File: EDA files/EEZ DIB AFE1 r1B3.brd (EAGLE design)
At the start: 141.5 x 68.5 mm, 198 parts, among them IC1 OPA4202IPWR, IC10 N.C., IC11 N.C., IC12 N.C., IC13 ADS131E04IPAGR, IC14 TPS71725DCKR, IC15 TPS72325DBVR, IC2 DG212BDY-T1-E3, IC3 ULN2803ADWR, IC4 OPA4202IPWR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

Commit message: small PCB layout changes
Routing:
- net GND: track 88.3 -> 86.8 mm, vias 66 -> 67
- net IN3P: track 39.7 -> 39.5 mm, vias 3 -> 2
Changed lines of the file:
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@@
 <layer number="13" name="Route13" color="4" fill="5" visible="no" active="no"/>
 <layer number="14" name="Route14" color="1" fill="6" visible="no" active="no"/>
-<layer number="15" name="Power" color="6" fill="1" visible="no" active="yes"/>
-<layer number="16" name="Bottom" color="1" fill="1" visible="no" active="yes"/>
+<layer number="15" name="Power" color="6" fill="1" visible="yes" active="yes"/>
+<layer number="16" name="Bottom" color="1" fill="1" visible="yes" active="yes"/>
 <layer number="17" name="Pads" color="14" fill="1" visible="yes" active="yes"/>
 <layer number="18" name="Vias" color="6" fill="1" visible="yes" active="yes"/>
@@
 <layer number="37" name="tTest" color="7" fill="1" visible="no" active="yes"/>
 <layer number="38" name="bTest" color="7" fill="1" visible="no" active="yes"/>
-<layer number="39" name="tKeepout" color="15" fill="1" visible="yes" active="yes"/>
+<layer number="39" name="tKeepout" color="15" fill="1" visible="no" active="yes"/>
 <layer number="40" name="bKeepout" color="5" fill="1" visible="no" active="yes"/>
 <layer number="41" name="tRestrict" color="4" fill="10" visible="no" active="yes"/>
@@
 <via x="55.4228" y="43.2181" extent="1-16" drill="0.4" shape="square"/>
 <via x="54.3941" y="41.6306" extent="1-16" drill="0.4" shape="square"/>
-<wire x1="102.2096" y1="40.9804" x2="105.0061" y2="40.9804" width="0.2032" layer="1"/>
 <wire x1="105.0061" y1="40.9804" x2="105.1941" y2="40.7924" width="0.2032" layer="1"/>
 <wire x1="124.5226" y1="21.5646" x2="124.5226" y2="20.7273" width="0.2032" layer="1"/>
@@
 <via x="89.9033" y="13.2715" extent="1-16" drill="0.4" shape="square"/>
 <contactref element="IC13" pad="41"/>
+<via x="103.1875" y="41.8592" extent="1-16" drill="0.4" shape="octagon"/>
+<wire x1="102.2096" y1="40.9804" x2="102.3087" y2="40.9804" width="0.254" layer="1"/>
+<wire x1="102.3087" y1="40.9804" x2="103.1875" y2="41.8592" width="0.254" layer="1"/>
 <wire x1="105.1814" y1="6.7818" x2="105.2004" y2="6.7867" width="0" layer="19" extent="1-1"/>
 <wire x1="104.3504" y1="5.1117" x2="104.3686" y2="5.1308" width="0" layer="19" extent="1-1"/>
@@
 <wire x1="77.4954" y1="27.4828" x2="77.4954" y2="29.6418" width="0.8128" layer="16"/>
 <wire x1="77.4954" y1="29.6418" x2="79.756" y2="31.9024" width="0.8128" layer="16"/>
-<wire x1="103.1875" y1="31.9024" x2="103.1875" y2="42.6593" width="0.8128" layer="15"/>
-<wire x1="103.1875" y1="42.6593" x2="101.3714" y2="44.4754" width="0.8128" layer="15"/>
+<wire x1="103.1875" y1="31.9024" x2="103.1875" y2="38.7477" width="0.8128" layer="15"/>
 <wire x1="98.552" y1="48.2346" x2="93.7641" y2="48.2346" width="0.508" layer="16"/>
 <wire x1="93.7641" y1="48.2346" x2="93.6371" y2="48.1076" width="0.508" layer="16"/>
 <wire x1="101.3714" y1="44.4754" x2="101.3714" y2="45.4152" width="0.508" layer="16"/>
 <wire x1="101.3714" y1="45.4152" x2="98.552" y2="48.2346" width="0.508" layer="16"/>
+<wire x1="101.3714" y1="44.4754" x2="101.3714" y2="40.5638" width="0.8128" layer="15"/>
+<wire x1="101.3714" y1="40.5638" x2="103.1875" y2="38.7477" width="0.8128" layer="15"/>
 </signal>
 <signal name="+3V3_ISO">
@@
 <wire x1="89.8271" y1="47.9171" x2="91.0971" y2="46.6471" width="0.2032" layer="1"/>
 <wire x1="91.0971" y1="46.609" x2="91.0971" y2="46.6471" width="0.2032" layer="1"/>
-<wire x1="90.4748" y1="44.3611" x2="90.9701" y2="44.8564" width="0.2032" layer="1"/>
-<wire x1="90.9701" y1="44.8564" x2="91.0971" y2="45.4787" width="0.2032" layer="1"/>
-<wire x1="86.7029" y1="40.8305" x2="88.2396" y2="42.3672" width="0.2032" layer="1"/>
-<wire x1="90.4748" y1="44.3611" x2="88.9381" y2="44.3611" width="0.2032" layer="1"/>
-<wire x1="88.9381" y1="44.3611" x2="88.2396" y2="43.6626" width="0.2032" layer="1"/>
-<wire x1="88.2396" y1="42.3672" x2="88.2396" y2="43.6626" width="0.2032" layer="1"/>
-<via x="90.932" y="44.5897" extent="1-16" drill="0.4" shape="octagon"/>
-<wire x1="90.9701" y1="44.8564" x2="90.9701" y2="44.6278" width="0.2032" layer="1"/>
-<wire x1="90.9701" y1="44.6278" x2="90.932" y2="44.5897" width="0.2032" layer="1"/>
+<wire x1="86.7029" y1="40.8305" x2="88.646" y2="42.7736" width="0.2032" layer="1"/>
 <wire x1="86.6902" y1="36.3728" x2="86.6902" y2="35.3773" width="0.254" layer="1"/>
 <wire x1="86.6902" y1="35.3773" x2="87.8967" y2="34.1708" width="0.254" layer="1"/>
 <wire x1="86.7029" y1="40.8305" x2="86.7029" y2="39.1668" width="0.2032" layer="1"/>
 <wire x1="86.7029" y1="39.1668" x2="86.6902" y2="39.1541" width="0.2032" layer="1"/>
+<wire x1="91.0971" y1="45.4787" x2="91.0971" y2="44.4246" width="0.2032" layer="1"/>
+<wire x1="91.0971" y1="44.4246" x2="90.805" y2="44.1325" width="0.2032" layer="1"/>
+<wire x1="90.805" y1="44.1325" x2="89.2048" y2="44.1325" width="0.2032" layer="1"/>
+<wire x1="89.2048" y1="44.1325" x2="88.646" y2="43.5737" width="0.2032" layer="1"/>
+<wire x1="88.646" y1="43.5737" x2="88.646" y2="42.7736" width="0.2032" layer="1"/>
 </signal>
 <signal name="IN3N">

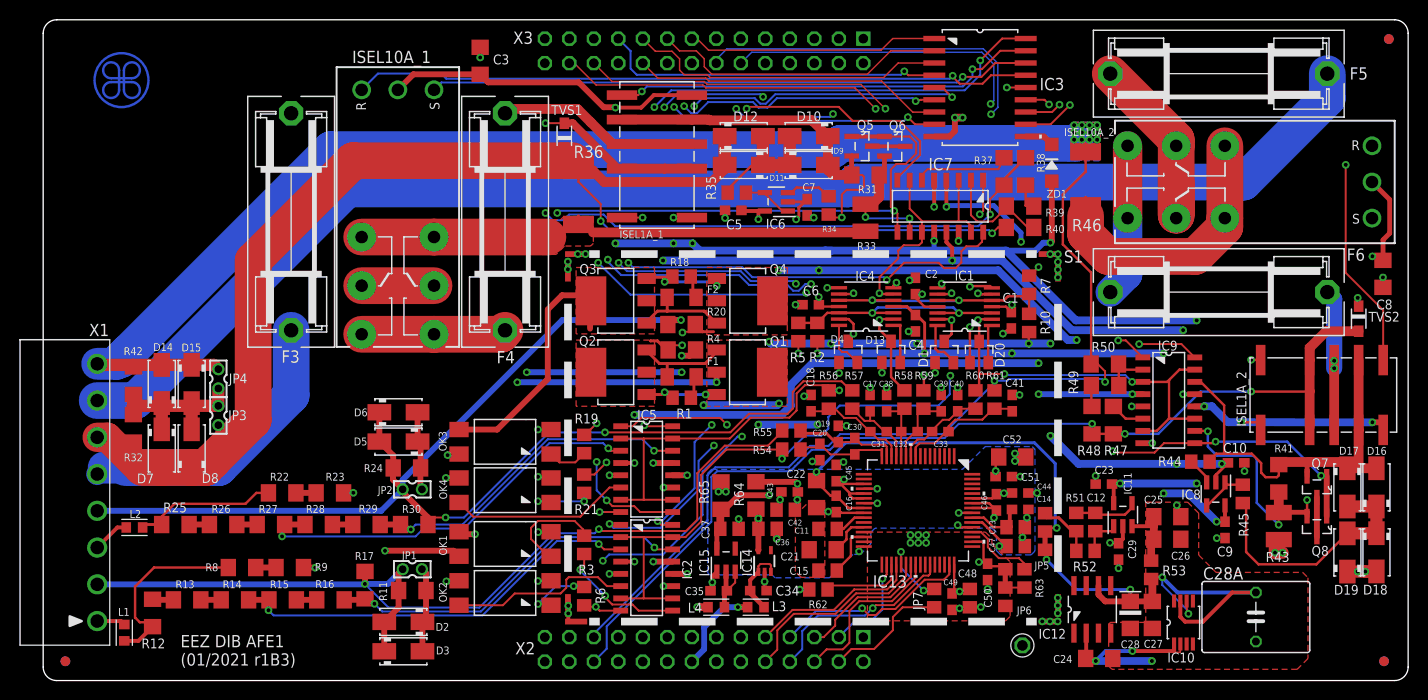
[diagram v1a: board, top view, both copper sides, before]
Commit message: PCB silkscreen fix
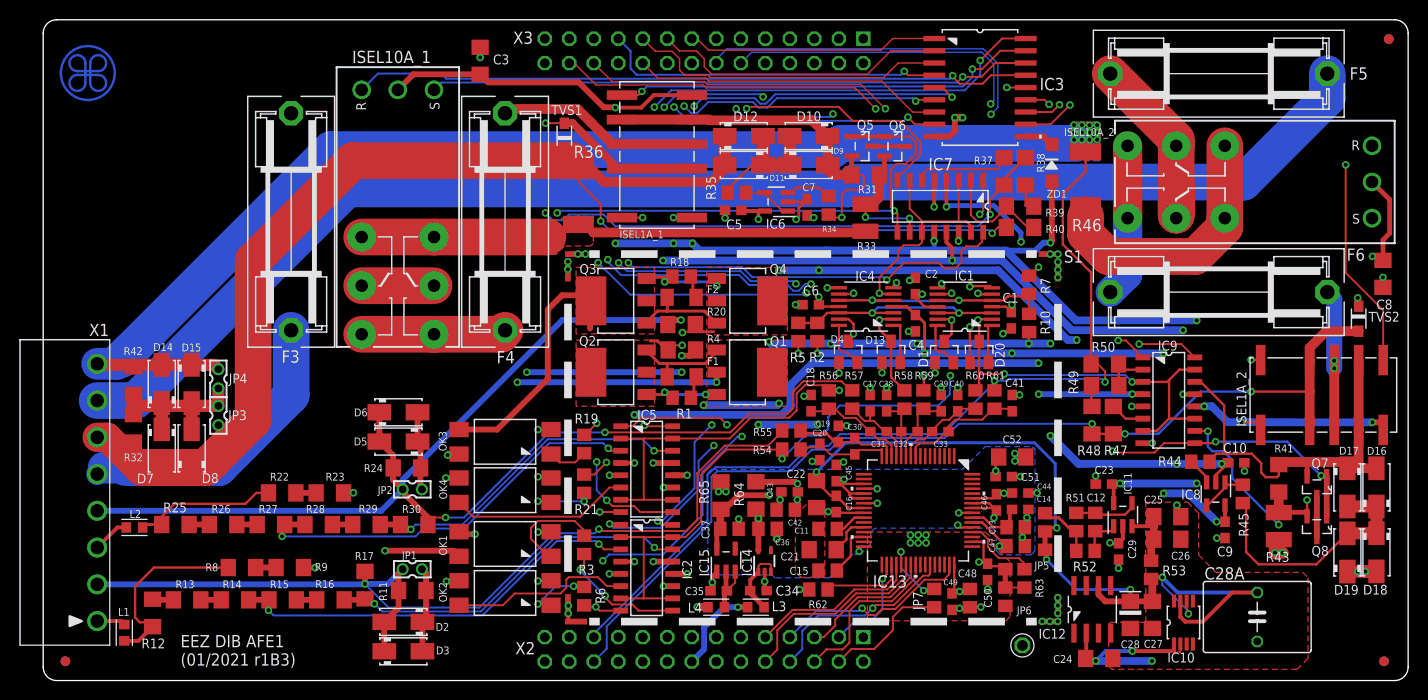
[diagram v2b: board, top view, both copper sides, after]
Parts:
- S1: value 2118732-2 -> N.C.
- moved EEZ_SIGNATURE 3.57 mm to (4.63, 62.0)
- moved C28A 0.14 mm to (125.9, 5.59)
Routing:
- net N$15: track 25.6 -> 24.1 mm
- net N$60: track 10.6 -> 11.7 mm
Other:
- board text added: "AIN1+ AIN1- AIN2+ AIN2- AIN3+ AIN3- AIN4+ AIN4-"
- board text added: "±2.4/48/240V ±48mA ±2.4/48/240V ±48mA ±48mA/1.2/10A ±2.4/12V ±48mA/1.2/10A ±2.4/12V"
- board text removed: "AIN1+ (Hi-volt) AIN1- AIN2+ (Hi-volt) AIN2- AIN3+ (Hi-curr) AIN3- AIN3+ (Hi-curr) AIN3-"

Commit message: active clamp op-amps changed
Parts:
- IC1, IC4: value OPA4202IPWR -> MCP6004T-I/ST
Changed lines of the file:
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@@
 <attribute name="VALUE" x="65.0113" y="27.9273" size="1.016" layer="27" ratio="10"/>
 </element>
-<element name="IC1" library="EEZ_TI" package="PW(R-PDSO-G14)" value="OPA4202IPWR" x="95.5294" y="37.7571" smashed="yes" rot="R180">
+<element name="IC1" library="EEZ_TI" package="PW(R-PDSO-G14)" value="MCP6004T-I/ST" x="95.5294" y="37.7571" smashed="yes" rot="R180">
 <attribute name="NAME" x="94.488" y="40.4749" size="1.016" layer="25" ratio="10"/>
 <attribute name="VALUE" x="92.6719" y="37.4015" size="0.6096" layer="27" ratio="10"/>
@@
 <attribute name="VALUE" x="64.8589" y="40.386" size="1.016" layer="27" ratio="10"/>
 </element>
-<element name="IC4" library="EEZ_TI" package="PW(R-PDSO-G14)" value="OPA4202IPWR" x="85.3186" y="37.7698" smashed="yes" rot="R180">
+<element name="IC4" library="EEZ_TI" package="PW(R-PDSO-G14)" value="MCP6004T-I/ST" x="85.3186" y="37.7698" smashed="yes" rot="R180">
 <attribute name="NAME" x="84.1883" y="40.4368" size="1.016" layer="25" ratio="10"/>
 <attribute name="VALUE" x="82.296" y="37.4523" size="0.6096" layer="27" ratio="10"/>
